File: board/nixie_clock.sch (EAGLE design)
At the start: 41 parts, among them Q1 BC546B, U1 AMS1117-5.0, U2 SN74141N

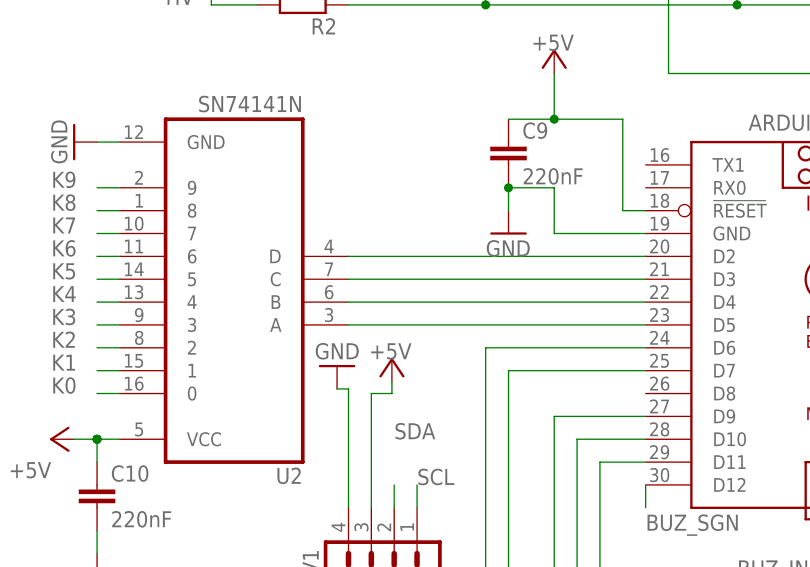
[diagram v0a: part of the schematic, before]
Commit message: added nixie tube testing script.
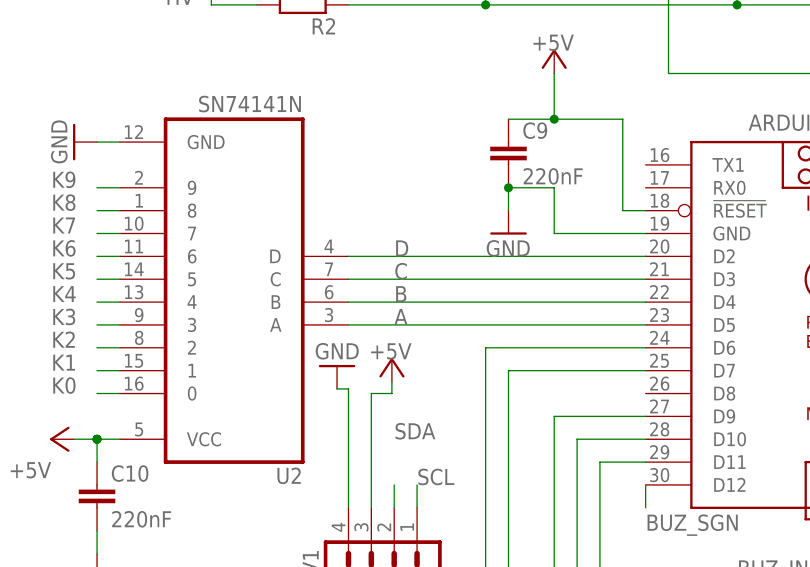
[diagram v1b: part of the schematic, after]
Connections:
- net N$11 renamed D
- net N$12 renamed C
- net N$13 renamed B
- net N$14 renamed A
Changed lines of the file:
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@@
 </segment>
 </net>
-<net name="N$11" class="0">
+<net name="D" class="0">
 <segment>
 <pinref part="U2" gate="G$1" pin="D"/>
 <pinref part="ARDUINO_NANO" gate="G$1" pin="D2"/>
 <wire x1="297.18" y1="106.68" x2="330.2" y2="106.68" width="0.1524" layer="91"/>
+<label x="302.26" y="106.68" size="1.778" layer="95"/>
 </segment>
 </net>
-<net name="N$12" class="0">
+<net name="C" class="0">
 <segment>
 <pinref part="U2" gate="G$1" pin="C"/>
 <pinref part="ARDUINO_NANO" gate="G$1" pin="D3"/>
 <wire x1="297.18" y1="104.14" x2="330.2" y2="104.14" width="0.1524" layer="91"/>
+<label x="302.26" y="104.14" size="1.778" layer="95"/>
 </segment>
 </net>
-<net name="N$13" class="0">
+<net name="B" class="0">
 <segment>
 <pinref part="U2" gate="G$1" pin="B"/>
 <pinref part="ARDUINO_NANO" gate="G$1" pin="D4"/>
 <wire x1="297.18" y1="101.6" x2="330.2" y2="101.6" width="0.1524" layer="91"/>
+<label x="302.26" y="101.6" size="1.778" layer="95"/>
 </segment>
 </net>
-<net name="N$14" class="0">
+<net name="A" class="0">
 <segment>
 <pinref part="U2" gate="G$1" pin="A"/>
 <pinref part="ARDUINO_NANO" gate="G$1" pin="D5"/>
 <wire x1="297.18" y1="99.06" x2="330.2" y2="99.06" width="0.1524" layer="91"/>
+<label x="302.26" y="99.06" size="1.778" layer="95"/>
 </segment>
 </net>
